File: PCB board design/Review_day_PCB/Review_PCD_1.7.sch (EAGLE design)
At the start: 10 parts, among them Q1 16 MHz, Q2 2N7000, U1 ATMEGA328P_VQFNVQFN

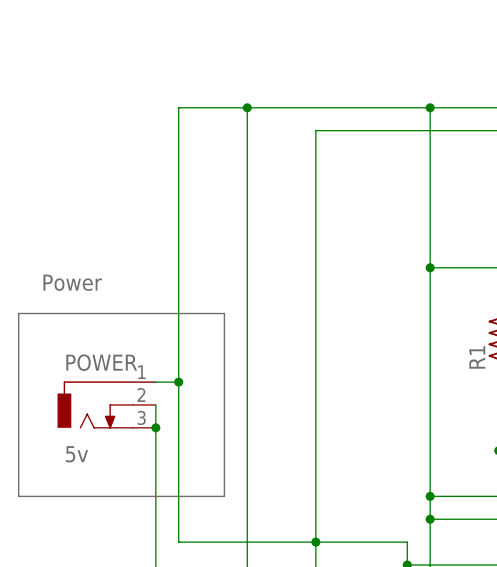
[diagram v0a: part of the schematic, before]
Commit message: cleared fixable errors
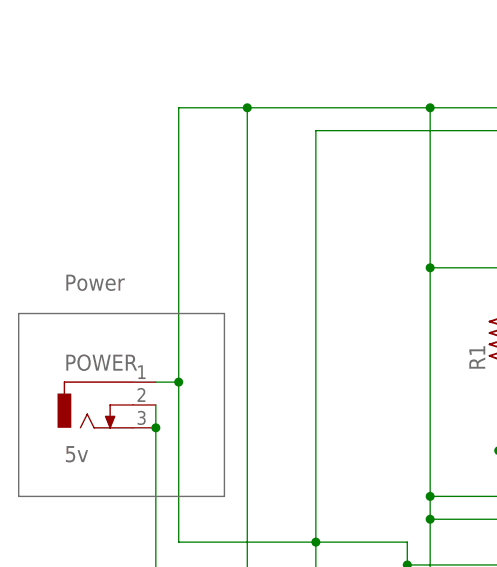
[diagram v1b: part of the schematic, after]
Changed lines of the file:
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@@
 <part name="JP3" library="adafruit" library_urn="urn:adsk.eagle:library:420" deviceset="PINHD-1X18" device="" package3d_urn="urn:adsk.eagle:package:6240826/1" value="Pinout to LCD"/>
 <part name="POWER" library="con-jack" library_urn="urn:adsk.eagle:library:154" deviceset="DCJ0202" device="" package3d_urn="urn:adsk.eagle:package:7491/1" value="5v"/>
-<part name="FRAME1" library="frames" library_urn="urn:adsk.eagle:library:229" deviceset="A4L-LOC" device=""/>
+<part name="FRAME1" library="frames" library_urn="urn:adsk.eagle:library:229" deviceset="A4L-LOC" device="" value="ABED Controller Frame"/>
 </parts>
 <sheets>
@@
 <wire x1="5.08" y1="96.52" x2="5.08" y2="76.2" width="0.1524" layer="95"/>
 <wire x1="5.08" y1="76.2" x2="-17.78" y2="76.2" width="0.1524" layer="95"/>
-<text x="-15.24" y="99.06" size="1.778" layer="95">Power</text>
+<text x="-12.7" y="99.06" size="1.778" layer="95">Power</text>
 <wire x1="104.14" y1="68.58" x2="104.14" y2="45.72" width="0.1524" layer="95"/>
 <wire x1="104.14" y1="45.72" x2="137.16" y2="45.72" width="0.1524" layer="95"/>

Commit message: navid saved the day
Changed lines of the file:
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@@
 <wire x1="15.24" y1="58.42" x2="15.24" y2="71.12" width="0.1524" layer="91"/>
 <wire x1="15.24" y1="71.12" x2="15.24" y2="116.84" width="0.1524" layer="91"/>
-<wire x1="0" y1="71.12" x2="15.24" y2="71.12" width="0.1524" layer="91"/>
+<wire x1="0" y1="71.12" x2="7.62" y2="71.12" width="0.1524" layer="91"/>
 <junction x="15.24" y="71.12"/>
+<wire x1="7.62" y1="71.12" x2="15.24" y2="71.12" width="0.1524" layer="91"/>
 <wire x1="15.24" y1="71.12" x2="25.4" y2="71.12" width="0.1524" layer="91"/>
 <wire x1="25.4" y1="71.12" x2="25.4" y2="68.58" width="0.1524" layer="91"/>
@@
 <pinref part="JP1" gate="A" pin="2"/>
 <wire x1="30.48" y1="35.56" x2="7.62" y2="35.56" width="0.1524" layer="91"/>
-<wire x1="7.62" y1="35.56" x2="7.62" y2="119.38" width="0.1524" layer="91"/>
+<wire x1="7.62" y1="35.56" x2="7.62" y2="71.12" width="0.1524" layer="91"/>
 <junction x="7.62" y="119.38"/>
 <pinref part="U1" gate="G$1" pin="PC0(ADC0)"/>
+<wire x1="7.62" y1="71.12" x2="7.62" y2="119.38" width="0.1524" layer="91"/>
 <wire x1="106.68" y1="81.28" x2="99.06" y2="81.28" width="0.1524" layer="91"/>
 <pinref part="U1" gate="G$1" pin="AVCC"/>
@@
 <wire x1="210.82" y1="114.3" x2="210.82" y2="93.98" width="0.1524" layer="91"/>
 <junction x="210.82" y="93.98"/>
+<junction x="7.62" y="71.12"/>
 </segment>
 </net>
